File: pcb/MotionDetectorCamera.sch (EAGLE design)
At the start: 134 parts, among them J2 S-MOUNT-LENS-HOLDER, J3 MINI-USB-JACK, U1 LATTICE-ICE40HX4K-BG121, U10 NXP-NTB0102, U11 ON-NLAS3157, U12 ON-NLAS3157, U13 STM-STM32F730, U2 TI-TPS6280XYKAR, U22 TI-TPD4S012DRYR, U3 MICROSD-SOCKET, U4 TI-TPS6280XYKAR, U5 W989D6DBGX6I, U6 TI-TPS63805YFFR, U8 ON-AR0330CS1C12SPKA0, U9 TI-TMUX1574, X1 SITIME-SIT8021, X2 SITIME-SIT8021

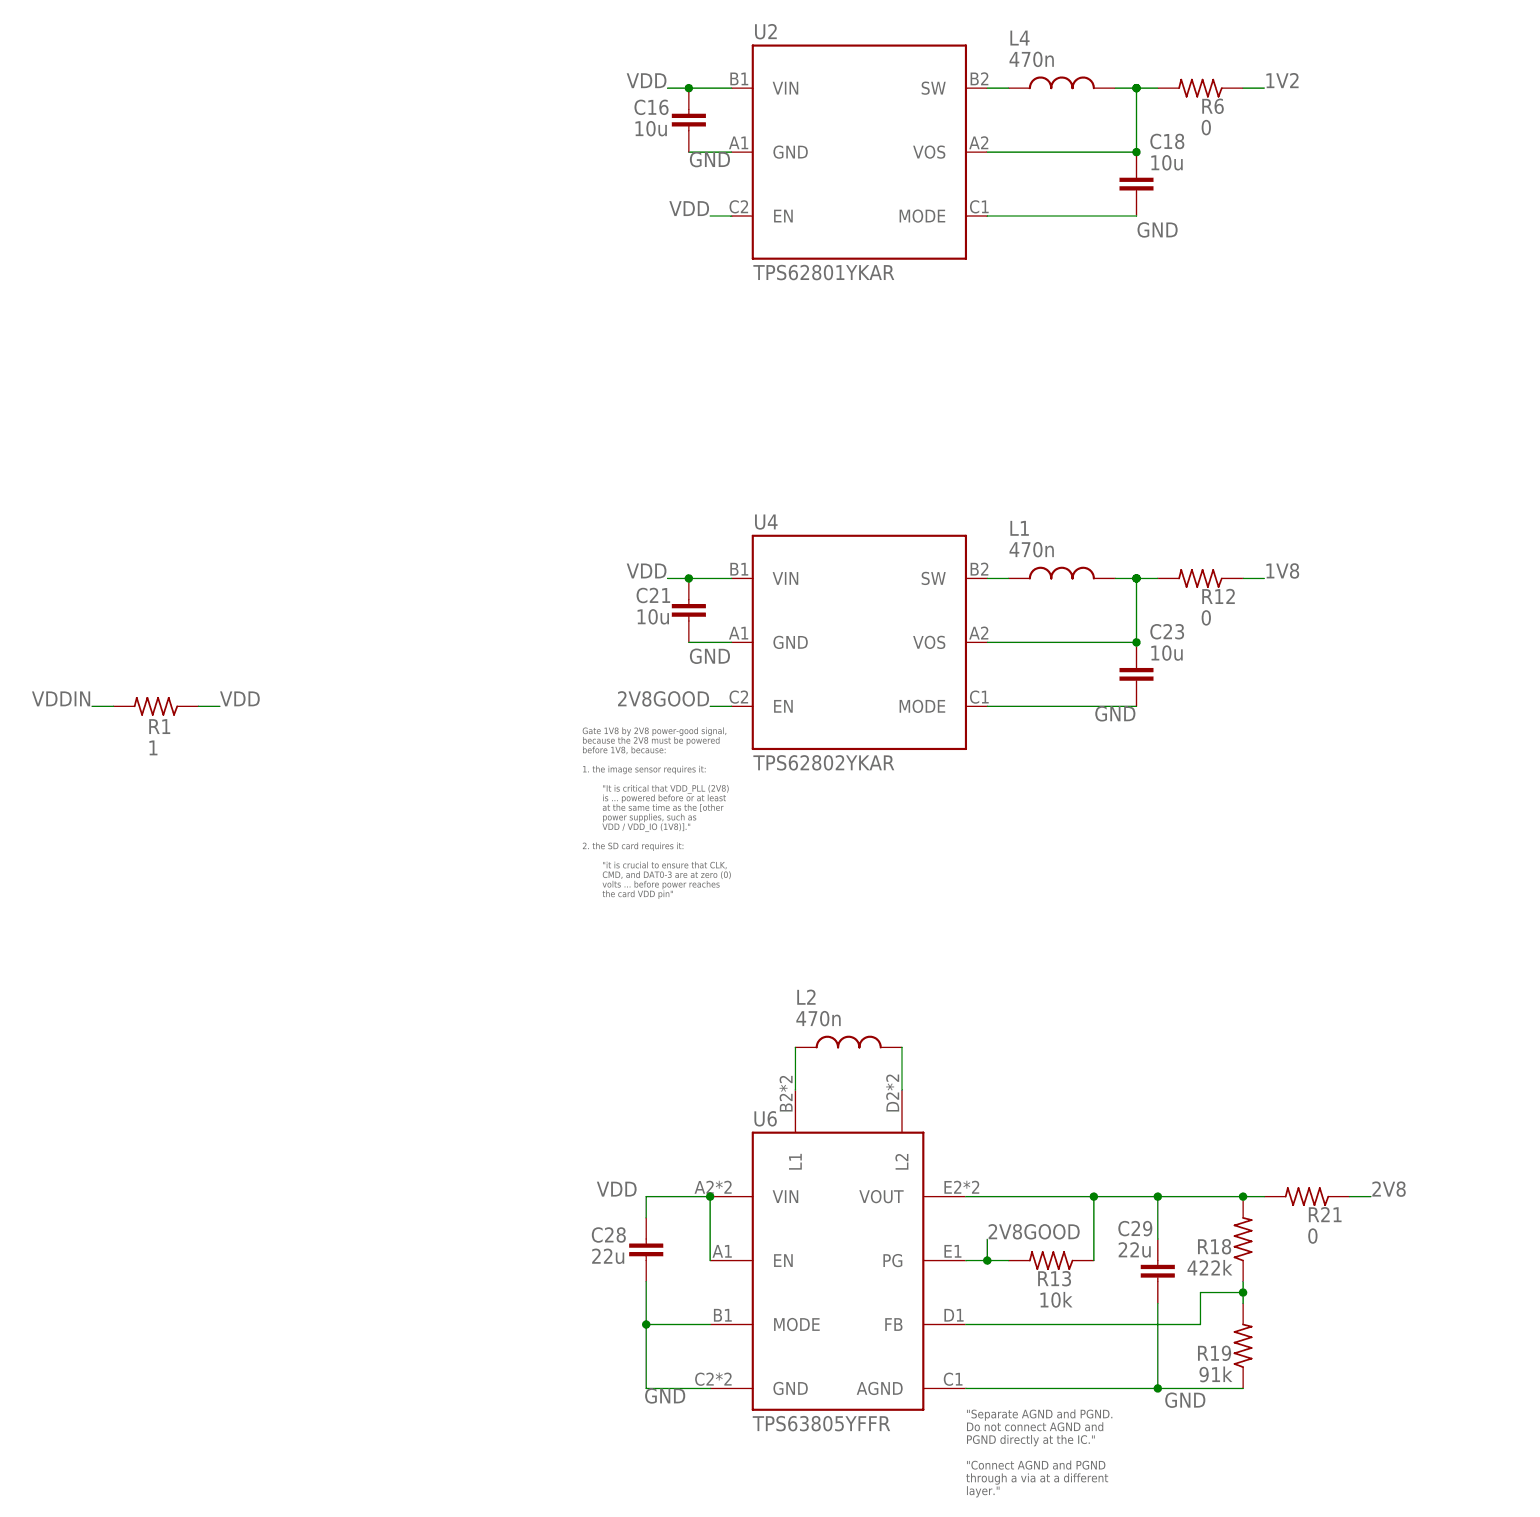
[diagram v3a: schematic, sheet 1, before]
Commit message: In the process of upgrading capacitors
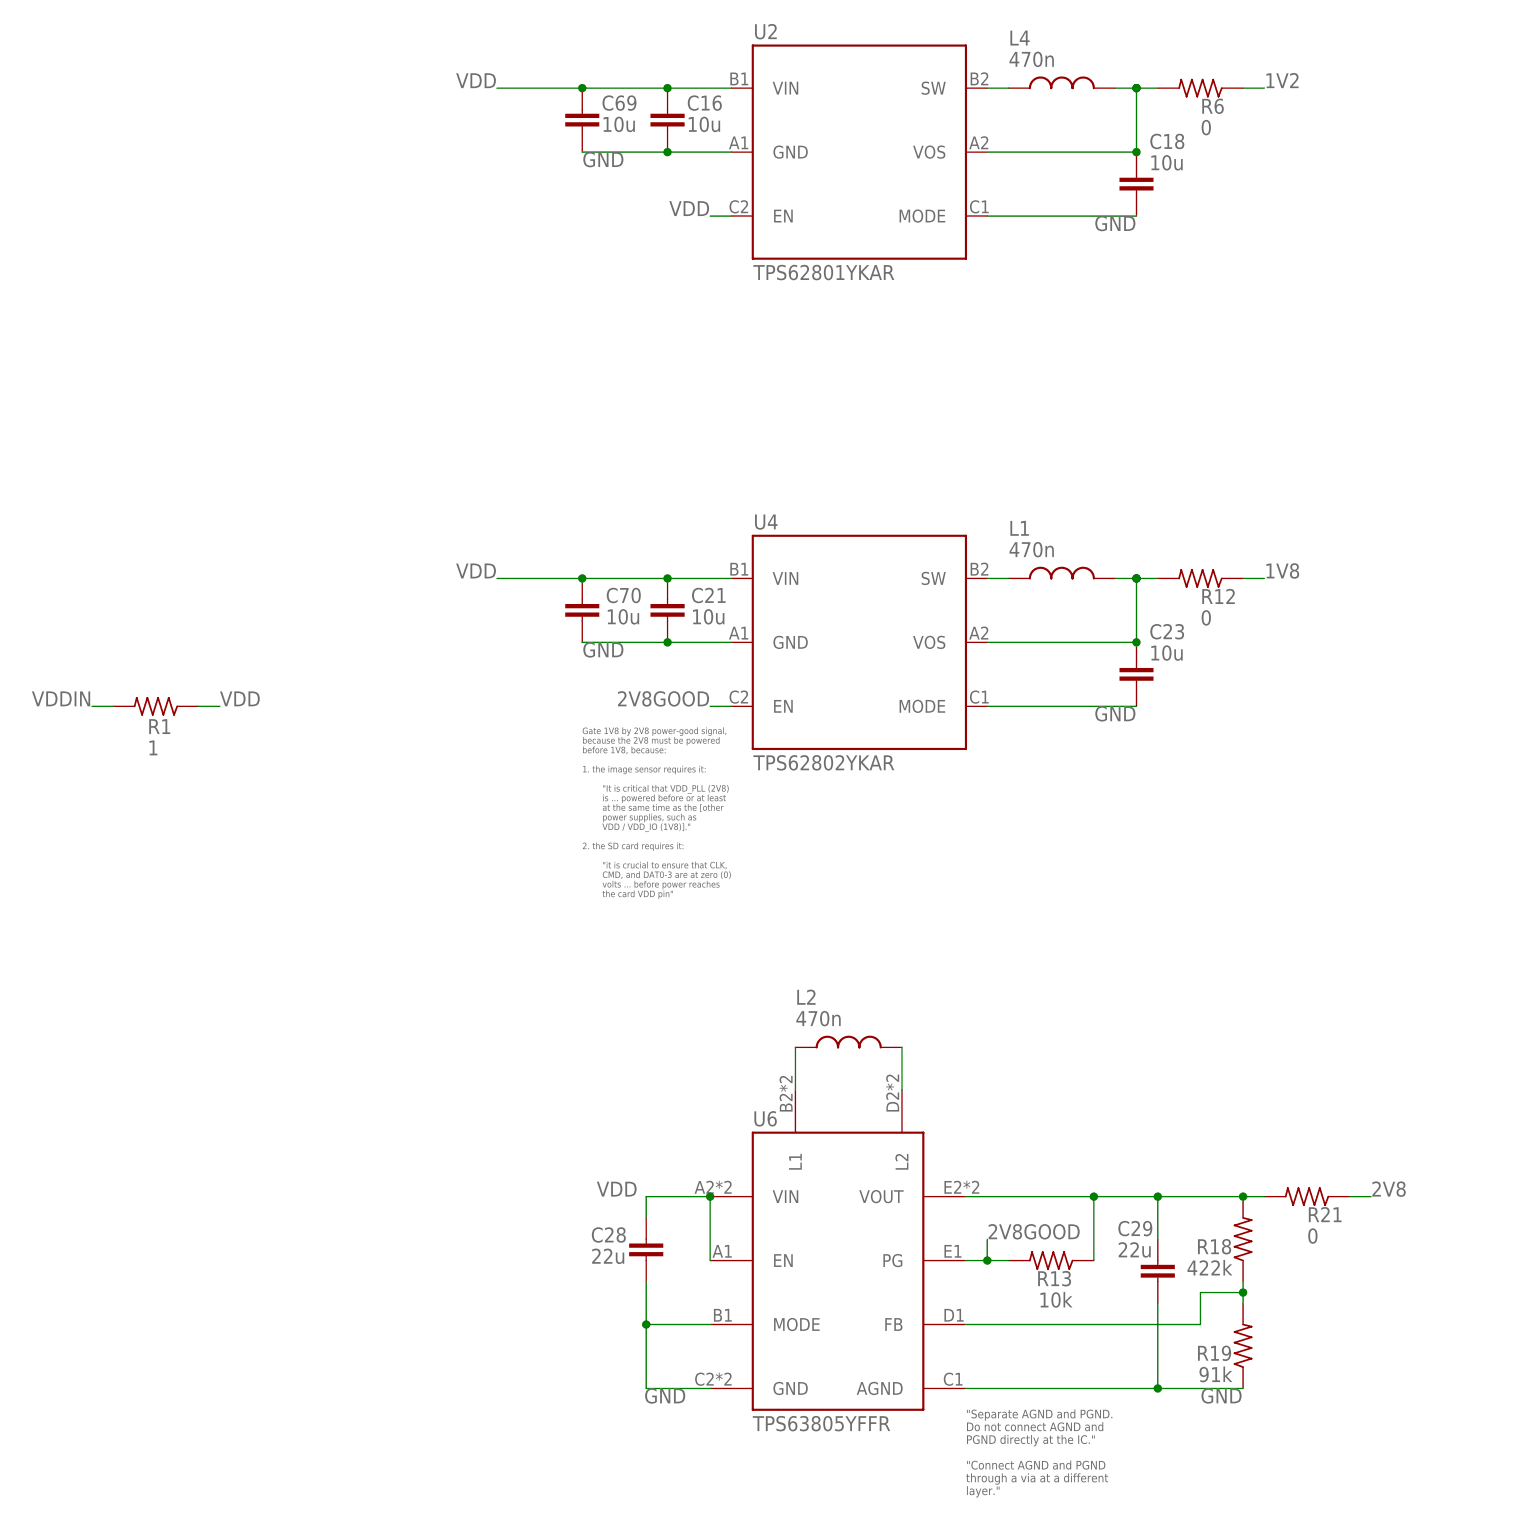
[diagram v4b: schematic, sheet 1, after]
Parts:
- added C69, C70: 10u, EagleLibrary:CAPACITOR0805
- C16, C18, C21, C23: device EagleLibrary:CAPACITOR0603 -> EagleLibrary:CAPACITOR0805; MFG Murata -> KEMET; PN GRM188R61A106KE69D -> C0805C106K8PACTU
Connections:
- net GND: now also C69.2, C70.2
- net VDD: now also C69.1, C70.1
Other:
- note added: "Keep these RC filter components small so they can be mounted below the chip."
- moved on the sheet: C16, C21

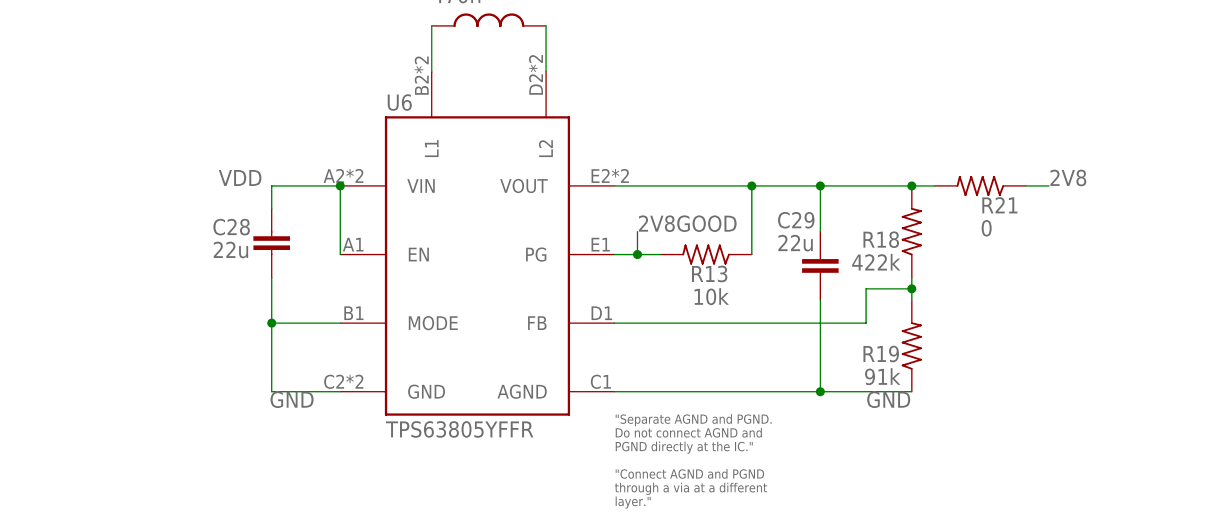
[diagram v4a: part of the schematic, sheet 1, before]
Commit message: In the process of upgrading capacitors
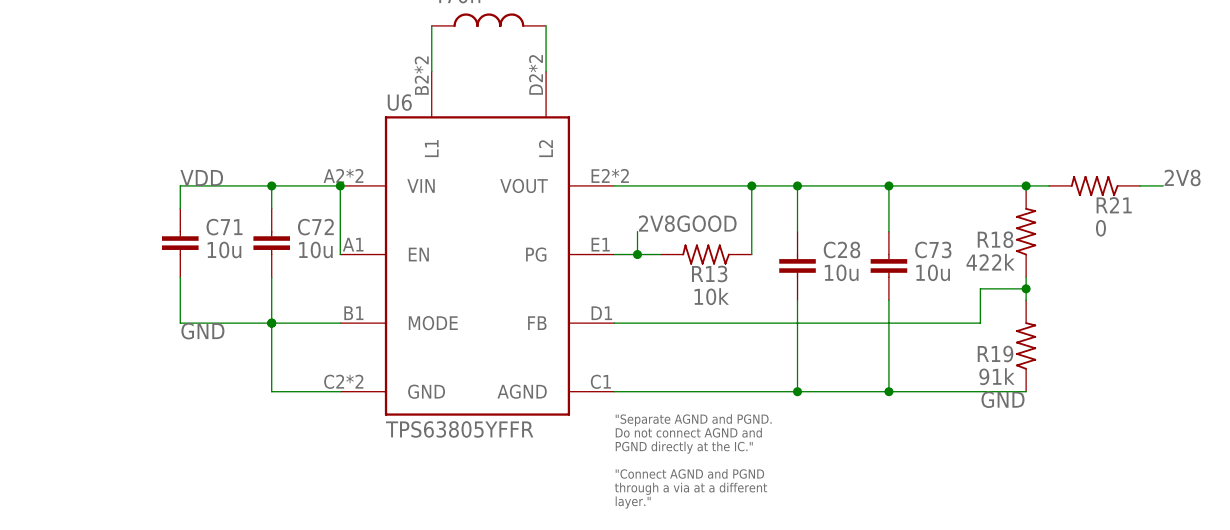
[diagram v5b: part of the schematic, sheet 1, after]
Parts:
- removed C29: 22u, EagleLibrary:CAPACITOR0805
- added C71, C72, C73: 10u, EagleLibrary:CAPACITOR0805
- C28: value 22u -> 10u; MFG Murata -> KEMET; PN GRM219R61C226ME15L -> C0805C106K8PACTU
- C32, C33, C34, C35, C36, C37: MFG Murata -> KEMET; PN GRM188R61A106KE69D -> C0805C106K8PACTU
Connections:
- net GND: now also C71.2, C72.2, C73.2; no longer C29.2
- net N$18: now also C28.1, C73.1; no longer C29.1
- net VDD: now also C71.1, C72.1; no longer C28.1
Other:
- moved on the sheet: C28, R18, R19, R21

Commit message: Commit before attempting to upgrade ice40 pll capactiors
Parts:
- C19, C24, C26: device EagleLibrary:CAPACITOR0603 -> EagleLibrary:CAPACITOR0805; MFG Murata -> KEMET; PN GRM188R61A106KE69D -> C0805C106K8PACTU
- C32, C33, C34, C35, C36, C37: device EagleLibrary:CAPACITOR0603 -> EagleLibrary:CAPACITOR0805
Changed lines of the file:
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@@
 </part>
 <part name="U5" library="EagleLibrary" deviceset="W989D6DBGX6I" device=""/>
-<part name="C24" library="EagleLibrary" deviceset="CAPACITOR" device="0603" value="10u">
-<spice>
-<pinmapping spiceprefix="C">
-<pinmap gate="G$1" pin="1" pinorder="1"/>
-<pinmap gate="G$1" pin="2" pinorder="2"/>
-</pinmapping>
-</spice>
-<attribute name="MFG" value="Murata"/>
-<attribute name="PN" value="GRM188R61A106KE69D"/>
+<part name="C24" library="EagleLibrary" deviceset="CAPACITOR" device="0805" value="10u">
+<spice>
+<pinmapping spiceprefix="C">
+<pinmap gate="G$1" pin="1" pinorder="1"/>
+<pinmap gate="G$1" pin="2" pinorder="2"/>
+</pinmapping>
+</spice>
+<attribute name="MFG" value="KEMET"/>
+<attribute name="PN" value="C0805C106K8PACTU"/>
 </part>
 <part name="C25" library="EagleLibrary" deviceset="CAPACITOR" device="0402" value="100n">
@@
 <attribute name="PN" value="GCM155R71H103JA55D"/>
 </part>
-<part name="C26" library="EagleLibrary" deviceset="CAPACITOR" device="0603" value="10u">
-<spice>
-<pinmapping spiceprefix="C">
-<pinmap gate="G$1" pin="1" pinorder="1"/>
-<pinmap gate="G$1" pin="2" pinorder="2"/>
-</pinmapping>
-</spice>
-<attribute name="MFG" value="Murata"/>
-<attribute name="PN" value="GRM188R61A106KE69D"/>
+<part name="C26" library="EagleLibrary" deviceset="CAPACITOR" device="0805" value="10u">
+<spice>
+<pinmapping spiceprefix="C">
+<pinmap gate="G$1" pin="1" pinorder="1"/>
+<pinmap gate="G$1" pin="2" pinorder="2"/>
+</pinmapping>
+</spice>
+<attribute name="MFG" value="KEMET"/>
+<attribute name="PN" value="C0805C106K8PACTU"/>
 </part>
 <part name="C27" library="EagleLibrary" deviceset="CAPACITOR" device="0402" value="100n">
@@
 <attribute name="PN" value="AR0330CS1C12SPKA0-CP2"/>
 </part>
-<part name="C32" library="EagleLibrary" deviceset="CAPACITOR" device="0603" value="10u">
+<part name="C32" library="EagleLibrary" deviceset="CAPACITOR" device="0805" value="10u">
 <attribute name="MFG" value="KEMET"/>
 <attribute name="PN" value="C0805C106K8PACTU"/>
@@
 <attribute name="PN" value="GRM155R61H104KE19D"/>
 </part>
-<part name="C33" library="EagleLibrary" deviceset="CAPACITOR" device="0603" value="10u">
+<part name="C33" library="EagleLibrary" deviceset="CAPACITOR" device="0805" value="10u">
 <attribute name="MFG" value="KEMET"/>
 <attribute name="PN" value="C0805C106K8PACTU"/>
@@
 <attribute name="PN" value="GRM155R61H104KE19D"/>
 </part>
-<part name="C34" library="EagleLibrary" deviceset="CAPACITOR" device="0603" value="10u">
+<part name="C34" library="EagleLibrary" deviceset="CAPACITOR" device="0805" value="10u">
 <attribute name="MFG" value="KEMET"/>
 <attribute name="PN" value="C0805C106K8PACTU"/>
@@
 <attribute name="PN" value="GRM155R61H104KE19D"/>
 </part>
-<part name="C36" library="EagleLibrary" deviceset="CAPACITOR" device="0603" value="10u">
+<part name="C36" library="EagleLibrary" deviceset="CAPACITOR" device="0805" value="10u">
 <attribute name="MFG" value="KEMET"/>
 <attribute name="PN" value="C0805C106K8PACTU"/>
@@
 <attribute name="PN" value="GRM155R61H104KE19D"/>
 </part>
-<part name="C37" library="EagleLibrary" deviceset="CAPACITOR" device="0603" value="10u">
+<part name="C37" library="EagleLibrary" deviceset="CAPACITOR" device="0805" value="10u">
 <attribute name="MFG" value="KEMET"/>
 <attribute name="PN" value="C0805C106K8PACTU"/>
@@
 <attribute name="PN" value="CRCW040210K0FKEDC"/>
 </part>
-<part name="C35" library="EagleLibrary" deviceset="CAPACITOR" device="0603" value="10u">
+<part name="C35" library="EagleLibrary" deviceset="CAPACITOR" device="0805" value="10u">
 <attribute name="MFG" value="KEMET"/>
 <attribute name="PN" value="C0805C106K8PACTU"/>
@@
 </part>
 <part name="U3" library="EagleLibrary" deviceset="MICROSD-SOCKET" device=""/>
-<part name="C19" library="EagleLibrary" deviceset="CAPACITOR" device="0603" value="10u">
-<attribute name="MFG" value="Murata"/>
-<attribute name="PN" value="GRM188R61A106KE69D"/>
+<part name="C19" library="EagleLibrary" deviceset="CAPACITOR" device="0805" value="10u">
+<attribute name="MFG" value="KEMET"/>
+<attribute name="PN" value="C0805C106K8PACTU"/>
 </part>
 <part name="C20" library="EagleLibrary" deviceset="CAPACITOR" device="0402" value="100n">

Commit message: Replaced ice40 pll capacitors with the same 10uF we're using everywhere else
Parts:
- C3, C4: device EagleLibrary:CAPACITOR0603 -> EagleLibrary:CAPACITOR0805; MFG Murata -> KEMET; PN GRM188R61A106KE69D -> C0805C106K8PACTU
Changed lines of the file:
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@@
 <attribute name="PN" value="CR0402AJW-101GAS"/>
 </part>
-<part name="C4" library="EagleLibrary" deviceset="CAPACITOR" device="0603" value="10u">
-<attribute name="MFG" value="Murata"/>
-<attribute name="PN" value="GRM188R61A106KE69D"/>
+<part name="C4" library="EagleLibrary" deviceset="CAPACITOR" device="0805" value="10u">
+<attribute name="MFG" value="KEMET"/>
+<attribute name="PN" value="C0805C106K8PACTU"/>
 </part>
 <part name="C11" library="EagleLibrary" deviceset="CAPACITOR" device="0402" value="100n">
@@
 <attribute name="PN" value="CR0402AJW-101GAS"/>
 </part>
-<part name="C3" library="EagleLibrary" deviceset="CAPACITOR" device="0603" value="10u">
-<attribute name="MFG" value="Murata"/>
-<attribute name="PN" value="GRM188R61A106KE69D"/>
+<part name="C3" library="EagleLibrary" deviceset="CAPACITOR" device="0805" value="10u">
+<attribute name="MFG" value="KEMET"/>
+<attribute name="PN" value="C0805C106K8PACTU"/>
 </part>
 <part name="C10" library="EagleLibrary" deviceset="CAPACITOR" device="0402" value="100n">
